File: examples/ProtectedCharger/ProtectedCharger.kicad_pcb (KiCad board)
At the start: 2 copper layers, 30 x 18 mm, 24 parts, among them J1 COM-15111, J2 S2B-PH-K, J3 S2B-PH-K, Q1 30V 4A 44m?@10V,4.3A 1.4W 1.3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, Q2 60V 5.2A 50m?@10V,3.2A 27W 2.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, Q3 20V 3.1A 860mW 112m?@4.5V,2.8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, U1 MCP73831T-2ACI/OT

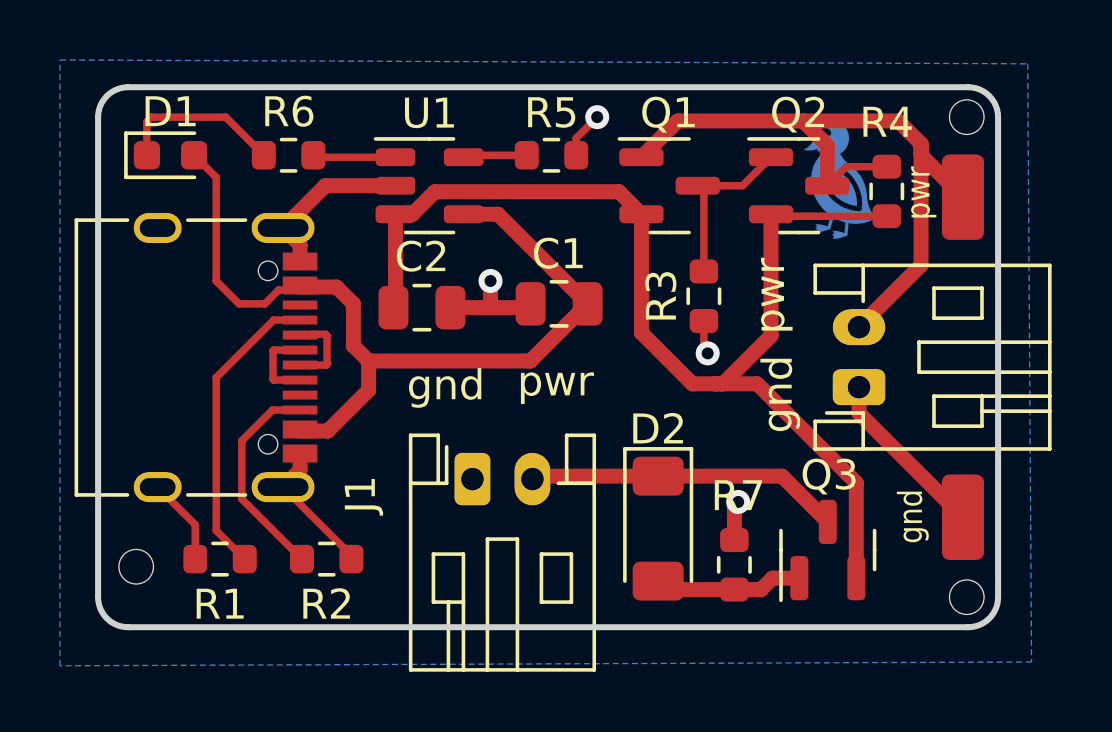
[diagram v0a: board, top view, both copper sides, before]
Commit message: Update: pwr_out (load) connector to use 3 pins instead Update: rearrange the board accordingly
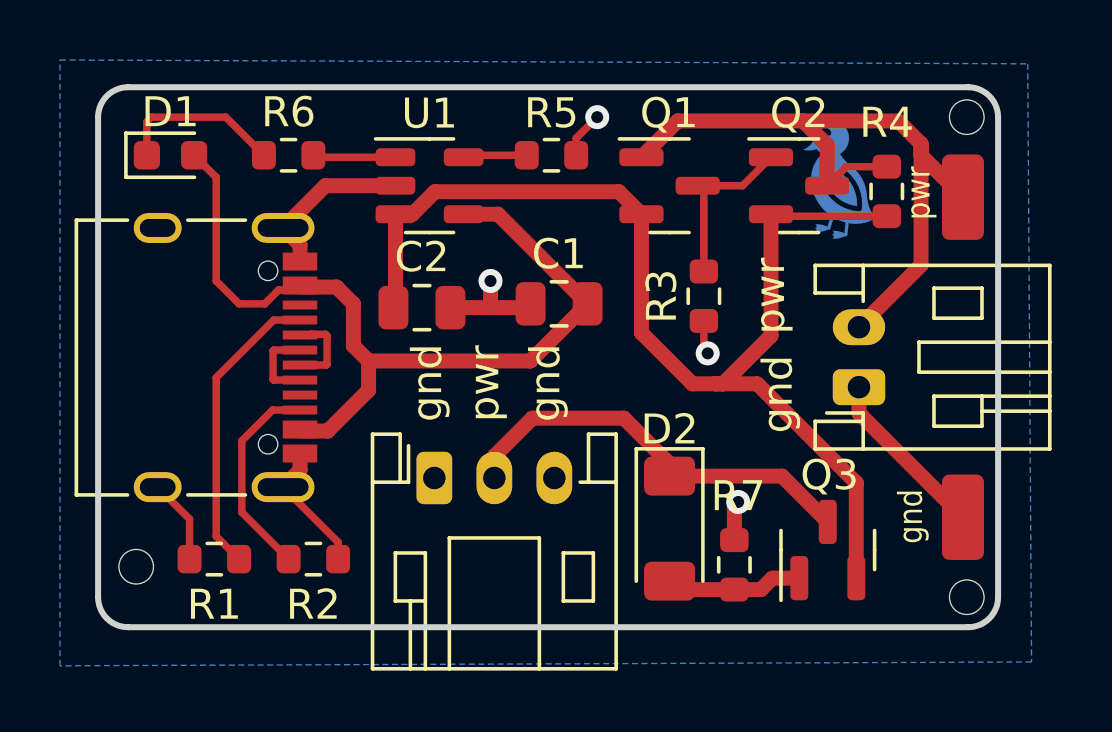
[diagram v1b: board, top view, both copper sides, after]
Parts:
- J3: value S2B-PH-K -> S3B-PH-K; footprint Connector_JST:JST_PH_S2B-PH-K_1x02_P2.00mm_Horizontal -> Connector_JST:JST_PH_S3B-PH-K_1x03_P2.00mm_Horizontal
- moved J3 1.27 mm to (75.2, 71.7)
- moved R2 0.44 mm to (71.2, 74.4)
- moved D2 0.38 mm to (83.1, 73.4)
- moved R1 0.19 mm to (67.9, 74.4)
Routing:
- net (adapter)pwr_pins.pins.2.src: track 10.5 -> 14.0 mm

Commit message: Update: the pcb board ports to flash with the edges
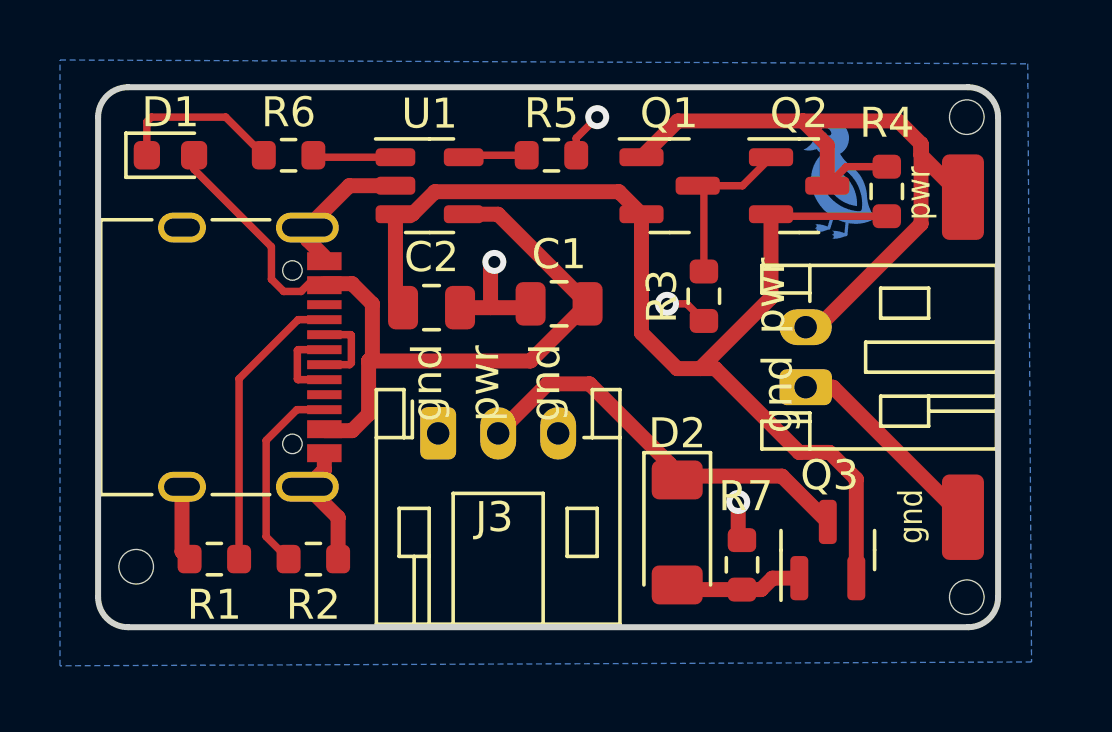
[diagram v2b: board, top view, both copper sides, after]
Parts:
- moved J2 1.78 mm to (87.6, 68.7)
- moved J3 1.49 mm to (75.3, 70.2)
- moved J1 0.81 mm to (67.9, 67.7)
- moved C2 0.32 mm to (75.1, 66.0)
- moved D2 0.28 mm to (83.3, 73.5)
- moved R7 0.25 mm to (85.5, 74.6)
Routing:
- net vusb: track 29.2 -> 28.0 mm
- net batt.pwr: track 24.2 -> 25.2 mm
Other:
- board text added: "Lipo 1 cell Charger ver. 1.1 PMOS Reverse Protection Test test_protected_charger.py"
- board text removed: "Lipo 1 cell Charger ver. 1.0 PMOS Reverse Protection Test test_protected_charger.py"
